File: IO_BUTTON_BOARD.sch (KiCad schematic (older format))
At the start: 33 parts

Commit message: Add reverse possibilities for pull-ups lanes
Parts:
- removed D?: PIN1, symbol LED_Small
- removed D?: PIN2, symbol LED_Small
- removed D?: PIN3, symbol LED_Small
- removed D?: PIN4, symbol LED_Small
- removed D?: PIN5, symbol LED_Small
- removed D?: PIN6, symbol LED_Small
- removed D?: PIN7, symbol LED_Small
- removed R? (x7): 1k, symbol R_Small
- removed SW?: SW1, symbol SW_PUSH_SMALL
- removed SW?: SW2, symbol SW_PUSH_SMALL
- removed SW?: SW3, symbol SW_PUSH_SMALL
- removed SW?: SW4, symbol SW_PUSH_SMALL
- removed SW?: SW5, symbol SW_PUSH_SMALL
- removed SW?: SW6, symbol SW_PUSH_SMALL
- removed SW?: SW7, symbol SW_PUSH_SMALL
- added D? (x8): PIN0_REV, symbol LED_Small
- added D? (x7): PIN0, symbol LED_Small
- added D?: LED_Small, symbol LED_Small
- added Q? (x3): NPN, symbol Q_NPN_BCE
- added Q? (x2): PNP, symbol Q_PNP_BCE
- added R? (x10): 1k, symbol R_Small
- added R? (x5): 10k, symbol R_Small
- added SW? (x7): SW0, symbol SW_PUSH_SMALL
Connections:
- net labels added: LANE_A, LANE_B, REVERSE_PULL
- net labels removed: +5VD
- wire segments 69 -> 142
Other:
- note added: "REVERSE ON => LANE_A = GND\nREVERSE OFF => LANE_B = VCC"
- moved on the sheet: C?, D?, P?, R?, SW?, SW?A, U?

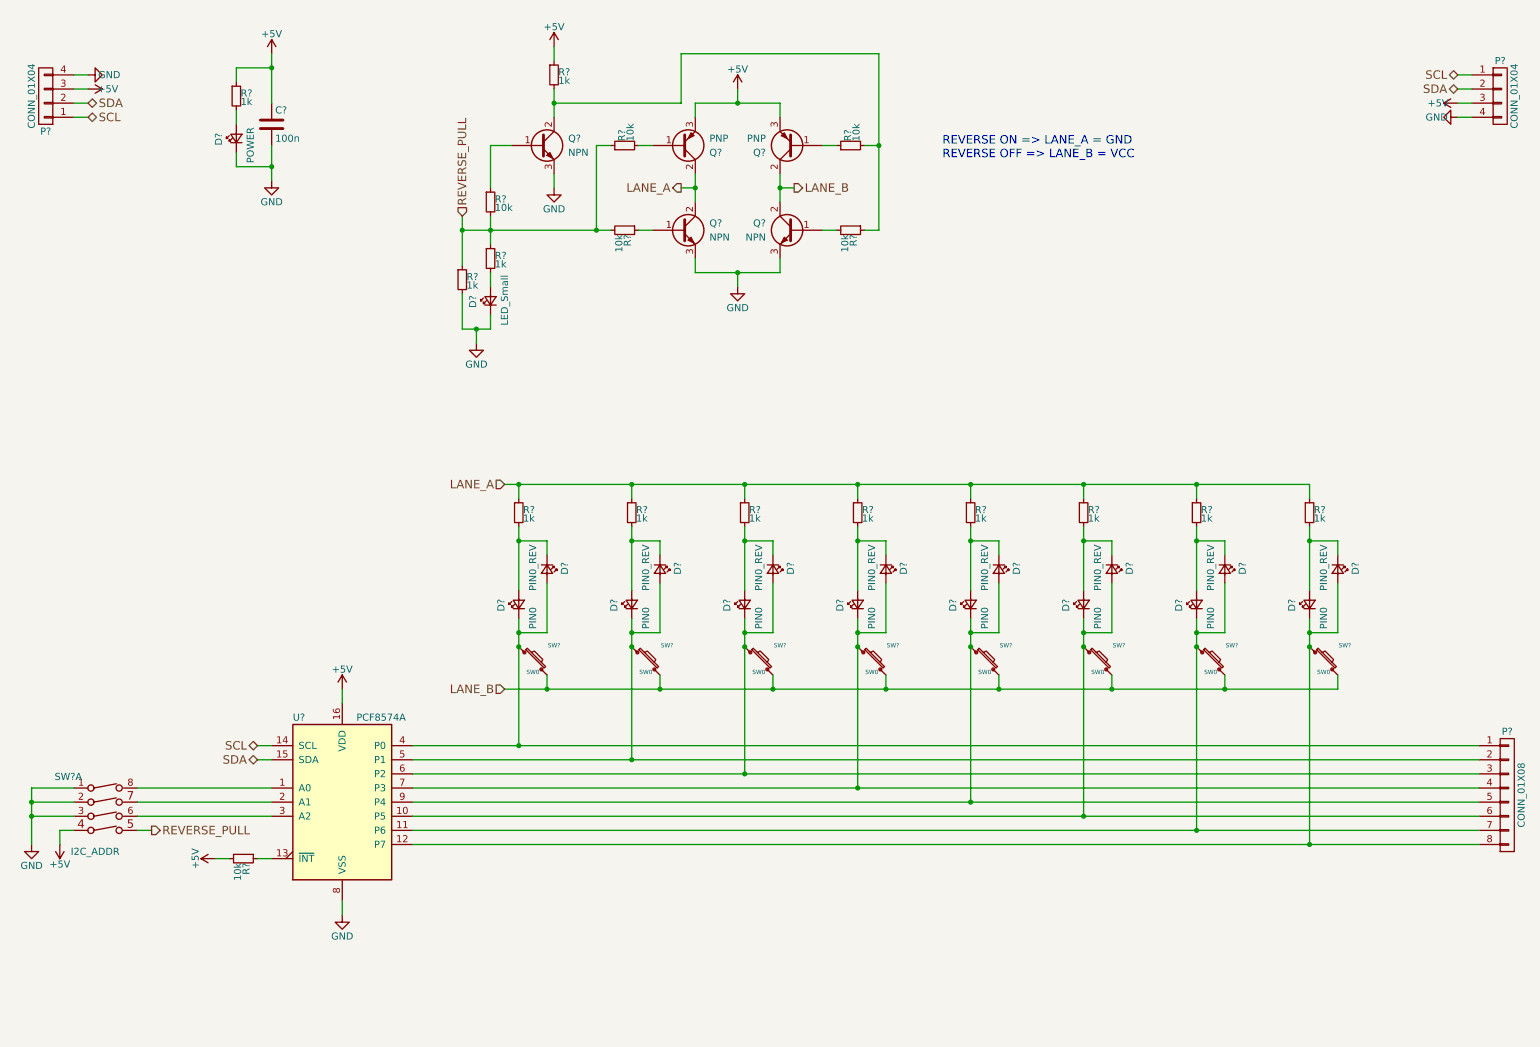
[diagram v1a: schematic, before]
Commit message: Add protection resistances Add logical gates to reverse logical signal Reduce number of leds
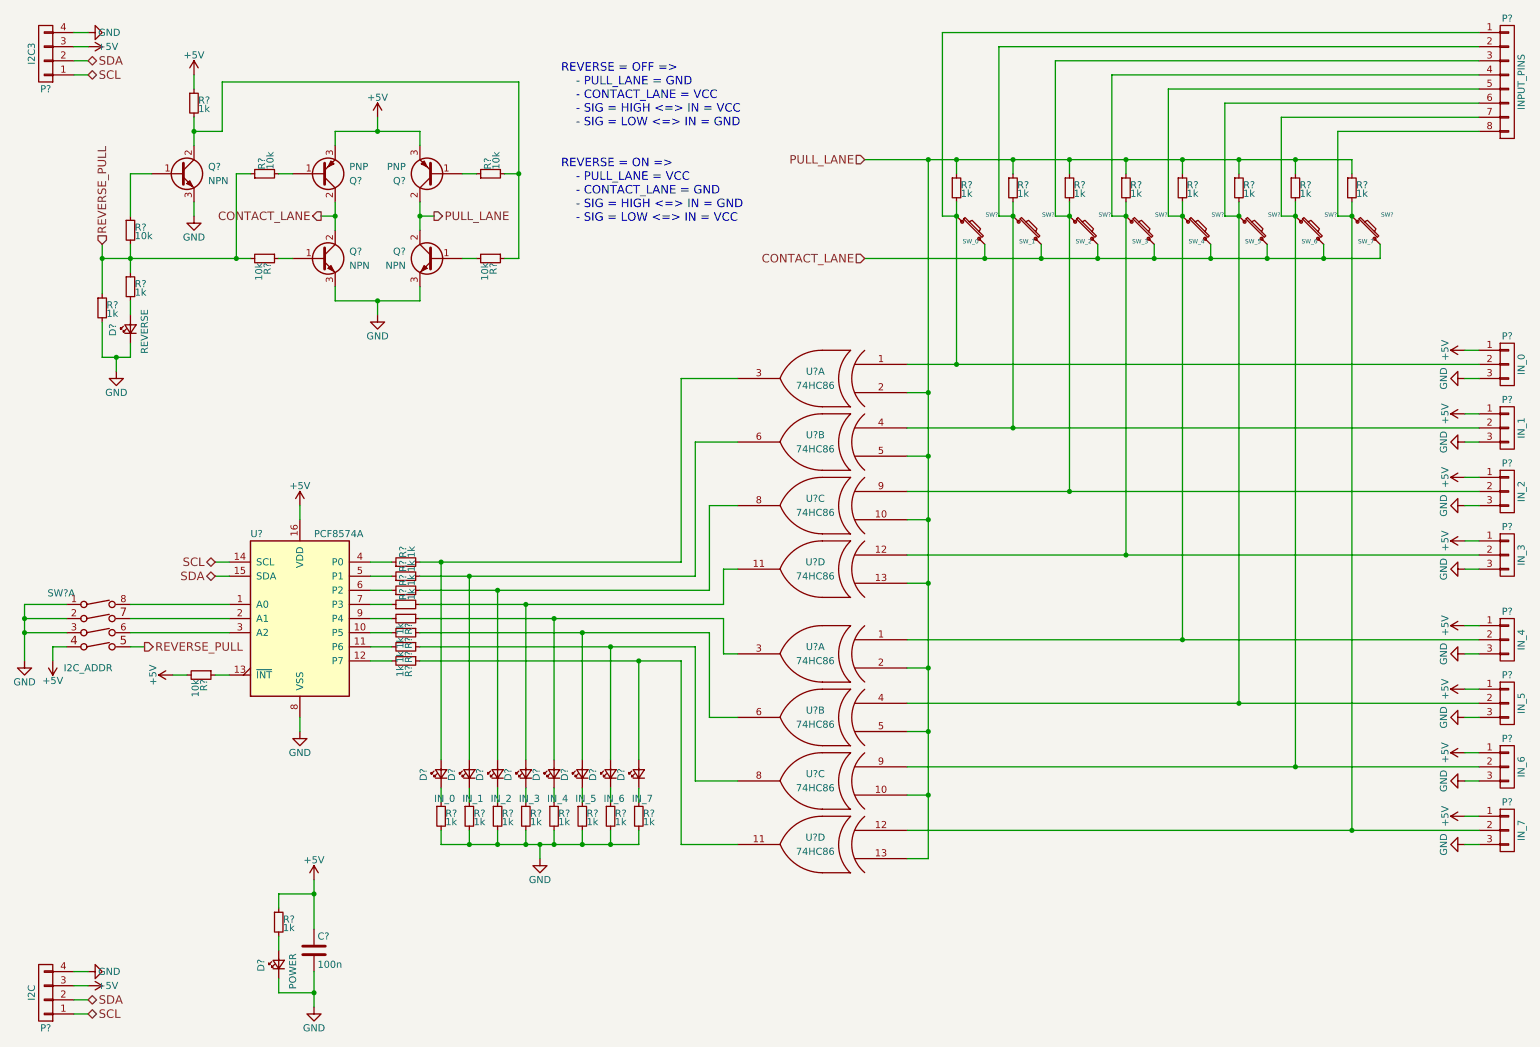
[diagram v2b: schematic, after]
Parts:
- removed D? (x8): PIN0, symbol LED_Small
- removed D? (x8): PIN0_REV, symbol LED_Small
- removed P?: CONN_01X08, symbol CONN_01X08
- added D?: IN_0, symbol LED_Small
- added D?: IN_1, symbol LED_Small
- added D?: IN_2, symbol LED_Small
- added D?: IN_3, symbol LED_Small
- added D?: IN_4, symbol LED_Small
- added D?: IN_5, symbol LED_Small
- added D?: IN_6, symbol LED_Small
- added D?: IN_7, symbol LED_Small
- added P?: IN_0, symbol CONN_01X03
- added P?: IN_1, symbol CONN_01X03
- added P?: IN_2, symbol CONN_01X03
- added P?: IN_3, symbol CONN_01X03
- added P?: IN_4, symbol CONN_01X03
- added P?: IN_5, symbol CONN_01X03
- added P?: IN_6, symbol CONN_01X03
- added P?: IN_7, symbol CONN_01X03
- added P?: INPUT_PINS, symbol CONN_01X08
- added R? (x16): 1k, symbol R_Small
- added U? (x8): 74HC86, symbol 74HC86
- D?: value LED_Small -> REVERSE
- P?: value CONN_01X04 -> I2C
- P?: value CONN_01X04 -> I2C3
- SW?: value SW0 -> SW_0
- SW?: value SW0 -> SW_1
- SW?: value SW0 -> SW_2
- SW?: value SW0 -> SW_3
- SW?: value SW0 -> SW_4
- SW?: value SW0 -> SW_5
- SW?: value SW0 -> SW_6
- SW?: value SW0 -> SW_7
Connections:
- net +5V: now also P?.1 (P1), P?.1 (P1), P?.1 (P1), P?.1 (P1), P?.1 (P1), P?.1 (P1), P?.1 (P1), P?.1 (P1)
- net GND: now also P?.3 (P3), P?.3 (P3), P?.3 (P3), P?.3 (P3), P?.3 (P3), P?.3 (P3), P?.3 (P3), P?.3 (P3), R?.2, R?.2, R?.2, R?.2, R?.2, R?.2, R?.2, R?.2, U?.7 (GND), U?.7 (GND), U?.7 (GND), U?.7 (GND), U?.7 (GND), U?.7 (GND), U?.7 (GND), U?.7 (GND)
- net at U?.10 (P5): now also R?.2; no longer SW?.1
- net at U?.11 (P6): now also R?.2; no longer SW?.1
- net at U?.12 (P7): now also R?.2; no longer SW?.1
- net at U?.4 (P0): now also R?.1; no longer SW?.1
- net at U?.5 (P1): now also R?.1; no longer SW?.1
- net at U?.6 (P2): now also R?.1; no longer SW?.1
- net at U?.7 (P3): now also R?.1; no longer SW?.1
- net at U?.9 (P4): now also R?.2; no longer SW?.1
- net at R?.2: now also SW?.1, P?.1 (P1), P?.2 (P2), U?.1 (IN1)
- net at R?.2: now also SW?.1, P?.2 (P2), P?.2 (P2), U?.4 (IN1)
- net at R?.2: now also SW?.1, P?.2 (P2), P?.3 (P3), U?.9 (IN1)
- net at R?.2: now also SW?.1, P?.2 (P2), P?.4 (P4), U?.12 (IN1)
- net at R?.2: now also SW?.1, P?.2 (P2), P?.5 (P5), U?.1 (IN1)
- net at R?.2: now also SW?.1, P?.2 (P2), P?.6 (P6), U?.4 (IN1)
- net at R?.2: now also SW?.1, P?.2 (P2), P?.7 (P7), U?.9 (IN1)
- net at R?.2: now also SW?.1, P?.2 (P2), P?.8 (P8), U?.12 (IN1)
- net LANE_A renamed PULL_LANE
- net PULL_LANE: now also Q?.2 (C), Q?.2 (C), U?.10 (IN2), U?.10 (IN2), U?.13 (IN2), U?.13 (IN2), U?.2 (IN2), U?.2 (IN2), U?.5 (IN2), U?.5 (IN2); no longer Q?.2 (C), Q?.2 (C)
- net LANE_B renamed CONTACT_LANE
- net CONTACT_LANE: now also Q?.2 (C), Q?.2 (C); no longer Q?.2 (C), Q?.2 (C)
- new net: D?.2 (A), R?.2, U?.3 (OUT)
- new net: D?.2 (A), R?.2, U?.6 (OUT)
- new net: D?.2 (A), R?.2, U?.8 (OUT)
- new net: D?.2 (A), R?.2, U?.11 (OUT)
- new net: D?.2 (A), R?.1, U?.3 (OUT)
- new net: D?.2 (A), R?.1, U?.6 (OUT)
- new net: D?.2 (A), R?.1, U?.8 (OUT)
- new net: D?.2 (A), R?.1, U?.11 (OUT)
- new net: D?.1 (K), R?.1 (x8)
- new net VCC: U?.14 (VCC), U?.14 (VCC), U?.14 (VCC), U?.14 (VCC), U?.14 (VCC), U?.14 (VCC), U?.14 (VCC), U?.14 (VCC)
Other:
- note added: "REVERSE = OFF =>\n - PULL_LANE = GND\n - CONTACT_LANE = VCC\n - SIG = HIGH <=> IN = VCC\n - SIG = LOW <=> IN = GND\n\n\nREVERSE = ON =>\n - PULL_LANE = VCC\n - CONTACT_LANE = GND\n - SIG = HIGH <=> IN = GND\n - SIG = LOW <=> IN = VCC"
- note removed: "REVERSE ON => LANE_A = GND\nREVERSE OFF => LANE_B = VCC"
- moved on the sheet: C?, D?, P?, Q?, R?, SW?, SW?A, U?

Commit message: Remove second connector
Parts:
- removed P?: INPUT_PINS, symbol CONN_01X08
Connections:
- wire segments 209 -> 193
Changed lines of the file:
@@
 Connection ~ 7550 3450
 Connection ~ 7150 3000
-$Comp
-L CONN_01X08 P?
-U 1 1 5C545CC4
-P 11050 1000
-F 0 "P?" H 11050 1450 50  0000 C CNN
-F 1 "INPUT_PINS" V 11150 1000 50  0000 C CNN
-F 2 "" H 11050 1000 50  0000 C CNN
-F 3 "" H 11050 1000 50  0000 C CNN
-	1    11050 1000
-	1    0    0    -1
-$EndComp
 Wire Wire Line
 	7150 1950 7050 1950
-Wire Wire Line
-	7050 1950 7050 650
-Wire Wire Line
-	7050 650  10850 650
-Wire Wire Line
-	10850 750  7450 750
-Wire Wire Line
-	7450 750  7450 1950
 Wire Wire Line
 	7450 1950 7550 1950
@@
 	7950 1950 7850 1950
 Wire Wire Line
-	7850 1950 7850 850
-Wire Wire Line
-	7850 850  10850 850
-Wire Wire Line
-	10850 950  8250 950
-Wire Wire Line
-	8250 950  8250 1950
-Wire Wire Line
 	8250 1950 8350 1950
 Wire Wire Line
 	8750 1950 8650 1950
-Wire Wire Line
-	8650 1950 8650 1050
-Wire Wire Line
-	8650 1050 10850 1050
-Wire Wire Line
-	10850 1150 9050 1150
-Wire Wire Line
-	9050 1150 9050 1950
 Wire Wire Line
 	9050 1950 9150 1950
@@
 	9550 1950 9450 1950
 Wire Wire Line
-	9450 1950 9450 1250
-Wire Wire Line
-	9450 1250 10850 1250
-Wire Wire Line
-	10850 1350 9850 1350
-Wire Wire Line
-	9850 1350 9850 1950
-Wire Wire Line
 	9850 1950 9950 1950

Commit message: Add switchs for input selection Add output PNP transistors Use Labels
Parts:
- removed P?: IN_0, symbol CONN_01X03
- removed P?: IN_1, symbol CONN_01X03
- removed P?: IN_2, symbol CONN_01X03
- removed P?: IN_3, symbol CONN_01X03
- removed P?: IN_4, symbol CONN_01X03
- removed P?: IN_5, symbol CONN_01X03
- removed P?: IN_6, symbol CONN_01X03
- removed P?: IN_7, symbol CONN_01X03
- removed Q? (x3): NPN, symbol Q_NPN_BCE
- removed Q? (x2): PNP, symbol Q_PNP_BCE
- added D?: OUT_0, symbol LED_Small
- added D?: OUT_1, symbol LED_Small
- added D?: OUT_2, symbol LED_Small
- added D?: OUT_3, symbol LED_Small
- added D?: OUT_4, symbol LED_Small
- added D?: OUT_5, symbol LED_Small
- added D?: OUT_6, symbol LED_Small
- added D?: OUT_7, symbol LED_Small
- added P? (x8): IO_0, symbol CONN_01X04
- added Q? (x3): NPN, symbol Q_NPN_BEC
- added Q? (x10): PNP, symbol Q_PNP_BCE
- added R? (x8): 10k, symbol R_Small
- added R? (x8): 1k, symbol R_Small
- added S? (x8): Switch2RT, symbol Switch2RT
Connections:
- net labels added: IN_0, IN_1, IN_2, IN_3, IN_4, IN_5, IN_6, IN_7, OUT_0, OUT_1, OUT_2, OUT_3, OUT_4, OUT_5, OUT_6, OUT_7
- wire segments 193 -> 267
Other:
- moved on the sheet: C?, D?, P?, R?, SW?, SW?A, U?, U?A, U?B, U?C, U?D
